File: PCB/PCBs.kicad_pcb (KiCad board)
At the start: 2 copper layers, 60 parts, among them CN2 W2A41C681KAT2A, CN5 W2A41C681KAT2A, CN6 W2A41C681KAT2A, CN7 W2A41C681KAT2A, J1 Conn_01x02_Pin, J2 Conn_01x10_Pin, J3 Conn_01x20_Socket, J4 Conn_01x20_Socket, U1 ADS1299IPAGR, U11 TPS73225DBVR, U3 TPD4E1B06DCKR, U4 TPD4E1B06DCKR, U5 LM2664M6, U6 TPS61023DRLR, U7 TPS73233DBVT, U8 TPS72325DBVT, U9 TPD4E1B06DCKR

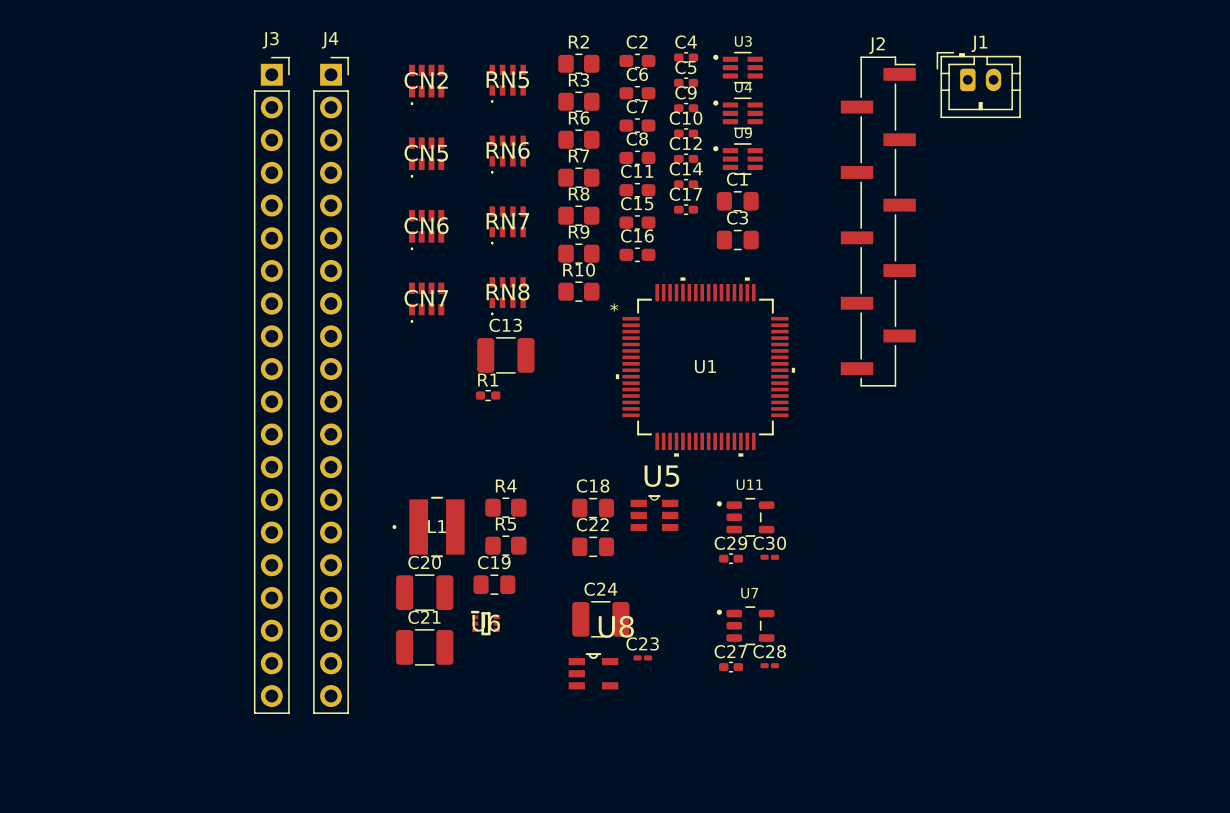
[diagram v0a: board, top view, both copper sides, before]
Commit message: pi socket spacing
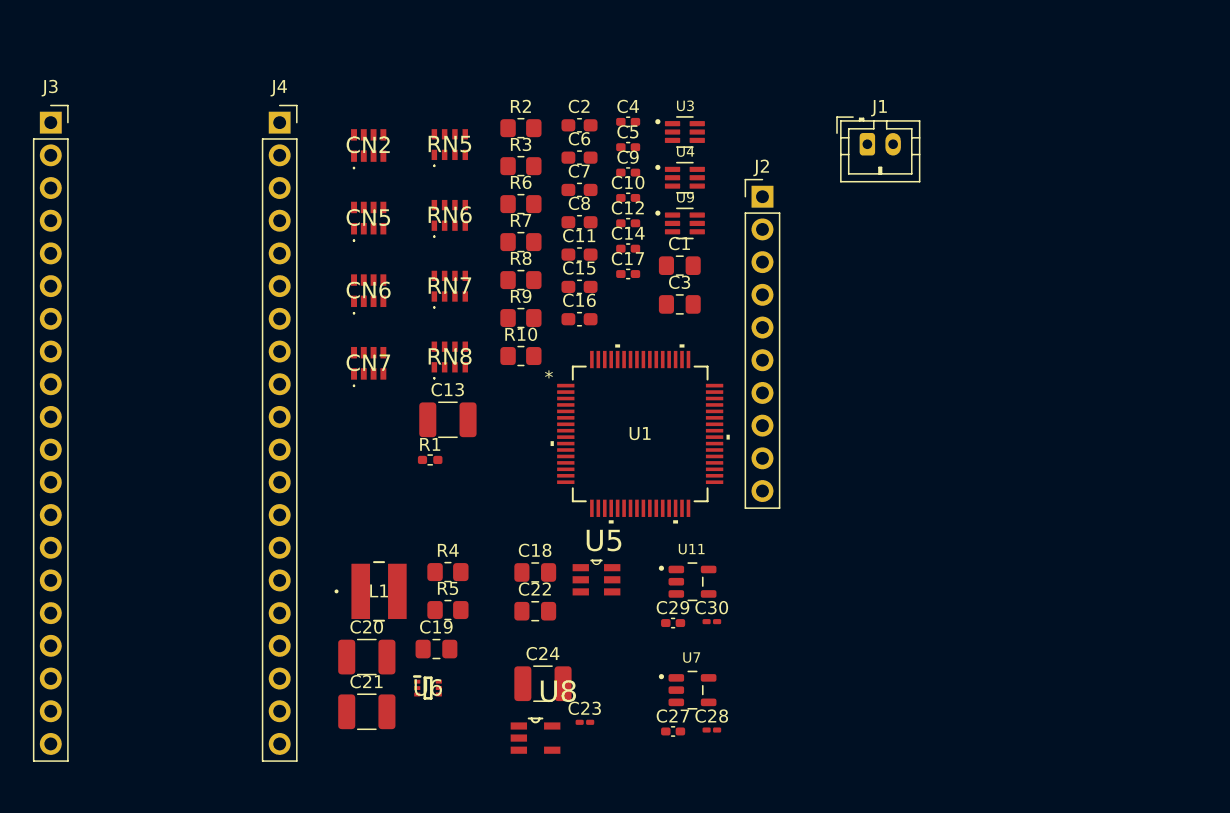
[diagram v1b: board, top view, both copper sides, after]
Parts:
- J2: footprint Connector_PinHeader_2.54mm:PinHeader_1x10_P2.54mm_Vertical_SMD_Pin1Right -> Connector_PinHeader_2.54mm:PinHeader_1x10_P2.54mm_Vertical
- moved J3 17.6 mm to (105.7, 60.3)
- moved J1 9.26 mm to (169.1, 62.0)
- moved J2 9.20 mm to (161.0, 66.1)
- moved U1 7.26 mm to (151.5, 84.5)
- moved R6 6.73 mm to (142.2, 66.7)
- moved RN6 6.73 mm to (136.7, 67.5)
- moved U9 6.73 mm to (155.0, 68.2)
- moved C1 6.73 mm to (154.6, 71.4)
- moved C10 6.73 mm to (150.6, 66.2)
- moved C11 6.73 mm to (146.8, 70.6)
- moved C12 6.73 mm to (150.6, 68.1)
- moved C13 6.73 mm to (136.6, 83.4)
- moved C14 6.73 mm to (150.6, 70.1)
- moved C15 6.73 mm to (146.8, 73.1)
- moved C16 6.73 mm to (146.8, 75.6)
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
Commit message: begining traces
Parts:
- moved J1 56.6 mm to (112.5, 62.0), turned to 180 degrees
- moved J2 54.1 mm to (127.5, 108.5), turned to 180 degrees
- moved C27 51.5 mm to (109.0, 82.6), turned to 90 degrees
- moved C29 49.6 mm to (109.0, 78.6), turned to 90 degrees
- moved C28 48.5 mm to (115.5, 82.4), turned to -90 degrees
- moved U7 48.5 mm to (112.2, 82.5)
- moved U11 46.7 mm to (112.2, 78.5)
- moved C30 46.5 mm to (115.4, 78.4), turned to -90 degrees
- moved C4 46.1 mm to (189.3, 85.3)
- moved C5 46.1 mm to (189.3, 87.2)
- moved C6 46.1 mm to (185.6, 88.0)
- moved C1 46.1 mm to (193.3, 96.4)
- moved C10 46.1 mm to (189.3, 91.2)
- moved C11 46.1 mm to (185.6, 95.6)
- moved C12 46.1 mm to (189.3, 93.1)
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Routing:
- net +5V: track 0.00 -> 61.5 mm
- net -2V5: track 0.00 -> 44.9 mm
- net +3V3: track 0.00 -> 34.9 mm
- net +2V5: track 0.00 -> 30.9 mm
- net Net-(U6-SW): track 0.00 -> 12.3 mm
- net /Booster/VBATT: track 0.00 -> 12.2 mm
- net -5V: track 0.00 -> 11.5 mm
- net Net-(U6-FB): track 0.00 -> 7.06 mm
- net Net-(U5-CAP-): track 0.00 -> 5.37 mm
- net Net-(U5-CAP+): track 0.00 -> 2.74 mm
- net Net-(U7-NR/FB): track 0.00 -> 2.27 mm
- net Net-(U11-NR/FB): track 0.00 -> 2.18 mm
- net Net-(U8-NR): track 0.00 -> 1.93 mm

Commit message: v0.1, pre-grounding
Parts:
- removed CN2, CN5, CN6, CN7: W2A41C681KAT2A, CustomLib:W3A41C102MAT2A
- added C25: 1nF, Capacitor_SMD:C_0603_1608Metric_Pad1.08x0.95mm_HandSolder, F.Cu at (147.4, 97.1)
- added C26: 1nF, Capacitor_SMD:C_0603_1608Metric_Pad1.08x0.95mm_HandSolder, F.Cu at (145.9, 97.1)
- added C31: 1nF, Capacitor_SMD:C_0603_1608Metric_Pad1.08x0.95mm_HandSolder, F.Cu at (144.8, 93.8)
- added C32: 1nF, Capacitor_SMD:C_0603_1608Metric_Pad1.08x0.95mm_HandSolder, F.Cu at (143.3, 93.8)
- added C33: 1nF, Capacitor_SMD:C_0603_1608Metric_Pad1.08x0.95mm_HandSolder, F.Cu at (142.2, 97.1)
- added C34: 1nF, Capacitor_SMD:C_0603_1608Metric_Pad1.08x0.95mm_HandSolder, F.Cu at (140.7, 97.1)
- added C35: 1nF, Capacitor_SMD:C_0603_1608Metric_Pad1.08x0.95mm_HandSolder, F.Cu at (139.9, 93.8)
- added C36: 1nF, Capacitor_SMD:C_0603_1608Metric_Pad1.08x0.95mm_HandSolder, F.Cu at (138.4, 93.8)
- added C37: 1nF, Capacitor_SMD:C_0603_1608Metric_Pad1.08x0.95mm_HandSolder, F.Cu at (136.9, 93.8)
- added C38: 1nF, Capacitor_SMD:C_0603_1608Metric_Pad1.08x0.95mm_HandSolder, F.Cu at (135.4, 93.8)
- added C39: 1nF, Capacitor_SMD:C_0603_1608Metric_Pad1.08x0.95mm_HandSolder, F.Cu at (134.7, 97.1)
- added C40: 1nF, Capacitor_SMD:C_0603_1608Metric_Pad1.08x0.95mm_HandSolder, F.Cu at (133.2, 97.1)
- added C41: 1nF, Capacitor_SMD:C_0603_1608Metric_Pad1.08x0.95mm_HandSolder, F.Cu at (132.1, 93.8)
- added C42: 1nF, Capacitor_SMD:C_0603_1608Metric_Pad1.08x0.95mm_HandSolder, F.Cu at (130.6, 93.8)
- added C43: 1nF, Capacitor_SMD:C_0603_1608Metric_Pad1.08x0.95mm_HandSolder, F.Cu at (129.5, 97.1)
- added C44: 1nF, Capacitor_SMD:C_0603_1608Metric_Pad1.08x0.95mm_HandSolder, F.Cu at (128.0, 97.1)
- added G***: LOGO, CustomLib:brain2, F.Cu at (145.7, 61.7)
- J2: value Conn_01x10_Pin -> Conn_01x09_Pin; footprint Connector_PinHeader_2.54mm:PinHeader_1x10_P2.54mm_Vertical -> Connector_PinHeader_2.54mm:PinHeader_1x09_P2.54mm_Vertical
- moved U9 66.6 mm to (127.2, 90.7), turned to 90 degrees
- moved C1 65.4 mm to (129.1, 84.1), turned to 180 degrees
- moved U4 63.2 mm to (132.4, 104.9), turned to 180 degrees
- moved C17 62.7 mm to (129.8, 77.3), turned to 180 degrees
- moved C16 60.4 mm to (129.3, 78.5), turned to 180 degrees
- moved C9 60.1 mm to (129.8, 81.0)
- moved C8 57.3 mm to (129.3, 82.3)
- moved R6 56.2 mm to (126.6, 77.6), turned to -90 degrees
- moved R10 55.9 mm to (127.6, 87.0), turned to 90 degrees
- moved C7 55.0 mm to (130.6, 87.2), turned to 180 degrees
- moved R9 54.9 mm to (133.8, 72.4), turned to 90 degrees
- moved U3 54.2 mm to (142.9, 104.9), turned to 180 degrees
- moved R8 51.8 mm to (135.7, 72.4), turned to 90 degrees
- moved R1 51.2 mm to (129.8, 85.6), turned to 180 degrees
- moved R2 50.7 mm to (130.4, 89.0)
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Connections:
- J2 pad 1: GND -> /ADS1299/Bias
- J2 pad 2: /ADS1299/Bias -> /ADS1299/I8
- J2 pad 3: /ADS1299/I8 -> /ADS1299/I7
- J2 pad 4: /ADS1299/I7 -> /ADS1299/I6
- J2 pad 5: /ADS1299/I6 -> /ADS1299/I5
- J2 pad 6: /ADS1299/I5 -> /ADS1299/I4
- J2 pad 7: /ADS1299/I4 -> /ADS1299/I3
- J2 pad 8: /ADS1299/I3 -> /ADS1299/I2
- J2 pad 9: /ADS1299/I2 -> /ADS1299/I1
- RN5 pad 1: /ADS1299/I8 -> /ADS1299/I1
- RN5 pad 2: /ADS1299/I7 -> /ADS1299/I8
- RN5 pad 3: /ADS1299/I7 -> /ADS1299/I8
- RN5 pad 4: /ADS1299/I6 -> /ADS1299/I7
- RN5 pad 5: /ADS1299/IN7N -> /ADS1299/IN7P
- RN5 pad 6: /ADS1299/IN7P -> /ADS1299/IN7N
- RN5 pad 7: /ADS1299/IN8N -> /ADS1299/IN8P
- RN5 pad 8: /ADS1299/IN8P -> /ADS1299/IN8N
- RN6 pad 1: /ADS1299/I6 -> /ADS1299/I7
- RN6 pad 2: /ADS1299/I5 -> /ADS1299/I6
- RN6 pad 3: /ADS1299/I5 -> /ADS1299/I6
- RN6 pad 4: /ADS1299/I4 -> /ADS1299/I5
- RN6 pad 5: /ADS1299/IN5N -> /ADS1299/IN5P
- RN6 pad 6: /ADS1299/IN5P -> /ADS1299/IN5N
- RN6 pad 7: /ADS1299/IN6N -> /ADS1299/IN6P
- RN6 pad 8: /ADS1299/IN6P -> /ADS1299/IN6N
- RN7 pad 1: /ADS1299/I4 -> /ADS1299/I5
- RN7 pad 2: /ADS1299/I3 -> /ADS1299/I4
- RN7 pad 3: /ADS1299/I3 -> /ADS1299/I4
- RN7 pad 4: /ADS1299/I2 -> /ADS1299/I3
- RN7 pad 5: /ADS1299/IN3N -> /ADS1299/IN3P
- RN7 pad 6: /ADS1299/IN3P -> /ADS1299/IN3N
- RN7 pad 7: /ADS1299/IN4N -> /ADS1299/IN4P
- RN7 pad 8: /ADS1299/IN4P -> /ADS1299/IN4N
- RN8 pad 1: /ADS1299/I2 -> /ADS1299/I3
- RN8 pad 2: /ADS1299/I1 -> /ADS1299/I2
- RN8 pad 3: /ADS1299/I1 -> /ADS1299/I2
- RN8 pad 4: /ADS1299/I8 -> /ADS1299/I1
- RN8 pad 5: /ADS1299/IN1N -> /ADS1299/IN1P
- RN8 pad 6: /ADS1299/IN1P -> /ADS1299/IN1N
- RN8 pad 7: /ADS1299/IN2N -> /ADS1299/IN2P
- RN8 pad 8: /ADS1299/IN2P -> /ADS1299/IN2N
- U3 pad 1: /ADS1299/I8 -> /ADS1299/I1
- U3 pad 2: /ADS1299/I1 -> /ADS1299/I2
- U3 pad 4: /ADS1299/I2 -> /ADS1299/I3
- U3 pad 5: /ADS1299/I3 -> /ADS1299/I4
- U4 pad 1: /ADS1299/I4 -> /ADS1299/I5
- U4 pad 2: /ADS1299/I5 -> /ADS1299/I6
- U4 pad 4: /ADS1299/I6 -> /ADS1299/I7
- U4 pad 5: /ADS1299/I7 -> /ADS1299/I8
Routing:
- net /ADS1299/CS: track 0.00 -> 52.9 mm, vias 0 -> 1
- net /ADS1299/MOSI: track 0.00 -> 51.5 mm, vias 0 -> 1
- net /ADS1299/PDWN: track 0.00 -> 47.6 mm, vias 0 -> 1
- net /ADS1299/RESET: track 0.00 -> 42.6 mm, vias 0 -> 1
- net /ADS1299/SCLK: track 0.00 -> 40.8 mm, vias 0 -> 1
- net /ADS1299/START: track 0.00 -> 37.5 mm, vias 0 -> 1
- net /ADS1299/I1: track 0.00 -> 34.2 mm
- net /ADS1299/Bias: track 0.00 -> 33.5 mm
- net +5V: track 61.5 -> 91.0 mm, vias 0 -> 1
- net +3V3: track 34.9 -> 11.1 mm
- net /ADS1299/I8: track 0.00 -> 18.7 mm
- net /ADS1299/IN1P: track 0.00 -> 16.5 mm, vias 0 -> 2
- net /ADS1299/IN8N: track 0.00 -> 16.2 mm, vias 0 -> 2
- net -2V5: track 44.9 -> 60.7 mm, vias 0 -> 8
- net /ADS1299/IN8P: track 0.00 -> 15.6 mm, vias 0 -> 2
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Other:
- board outline added: 45.5 x 52 mm
- board text added: "@jwmke"
- board text added: "B"
- board text added: "Made in USA"
- board text added: "Pi Pico EEG"
- board text added: "v0.1"

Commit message: layout additions
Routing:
- net +2V5: track 28.2 -> 63.0 mm, vias 0 -> 2
- net /ADS1299/MISO: track 1.94 -> 36.3 mm
- net /ADS1299/DRDY: track 1.66 -> 30.5 mm
- net +3V3: track 11.1 -> 36.8 mm, vias 0 -> 2
- net -2V5: track 60.7 -> 70.6 mm
- net /ADS1299/START: track 37.5 -> 38.8 mm

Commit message: v2 template
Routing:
- net GND: track 0.03 -> 79.9 mm, vias 0 -> 33
- net -2V5: track 70.6 -> 37.1 mm, vias 8 -> 9
- net /ADS1299/Bias: track 33.5 -> 35.1 mm
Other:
- copper layers 2 -> 4
